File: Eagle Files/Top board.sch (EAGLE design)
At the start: 3 parts, among them J1 MINI-USB-5P-3400030P1, U1 CN3065-1320040P1

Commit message: Tweak board
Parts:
- removed J2: (no value), Connector:JST-2P-SMD'2.0'
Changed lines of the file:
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@@
 <setting verticaltext="up"/>
 </settings>
-<grid distance="0.1" unitdist="inch" unit="inch" style="lines" multiple="1" display="no" altdistance="0.01" altunitdist="inch" altunit="inch"/>
+<grid distance="5" unitdist="mil" unit="mil" style="lines" multiple="1" display="no" altdistance="1" altunitdist="mil" altunit="mil"/>
 <layers>
 <layer number="1" name="Top" color="4" fill="1" visible="no" active="no"/>
@@
 <part name="U1" library="IC" deviceset="CN3065" device="-1320040P1"/>
 <part name="J1" library="Connector" deviceset="MINI-USB-5P" device="-3400030P1"/>
-<part name="J2" library="Connector" deviceset="JST-2P-SMD" device="'2.0'"/>
 </parts>
 <sheets>
@@
 <instance part="U1" gate="U" x="73.66" y="58.42"/>
 <instance part="J1" gate="USB" x="40.64" y="40.64"/>
-<instance part="J2" gate="G$1" x="78.74" y="22.86"/>
 </instances>
 <busses>

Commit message: Tweaks
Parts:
- added RD2007: RD2007, radiationbean:RD2007
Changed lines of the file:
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@@
 <setting verticaltext="up"/>
 </settings>
-<grid distance="5" unitdist="mil" unit="mil" style="lines" multiple="1" display="no" altdistance="1" altunitdist="mil" altunit="mil"/>
+<grid distance="0.1" unitdist="inch" unit="inch" style="lines" multiple="1" display="no" altdistance="0.01" altunitdist="inch" altunit="inch"/>
 <layers>
 <layer number="1" name="Top" color="4" fill="1" visible="no" active="no"/>
@@
 <part name="U1" library="IC" deviceset="CN3065" device="-1320040P1"/>
 <part name="J1" library="Connector" deviceset="MINI-USB-5P" device="-3400030P1"/>
+<part name="RD2007" library="radiationbean" deviceset="RD2007" device=""/>
 </parts>
 <sheets>
@@
 <instance part="U1" gate="U" x="73.66" y="58.42"/>
 <instance part="J1" gate="USB" x="40.64" y="40.64"/>
+<instance part="RD2007" gate="G$1" x="35.56" y="60.96"/>
 </instances>
 <busses>
@@
 </schematic>
 </drawing>
+<compatibility>
+<note version="6.3" minversion="6.2.2" severity="warning">
+Since Version 6.2.2 text objects can contain more than one line,
+which will not be processed correctly with this version.
+</note>
+</compatibility>
 </eagle>

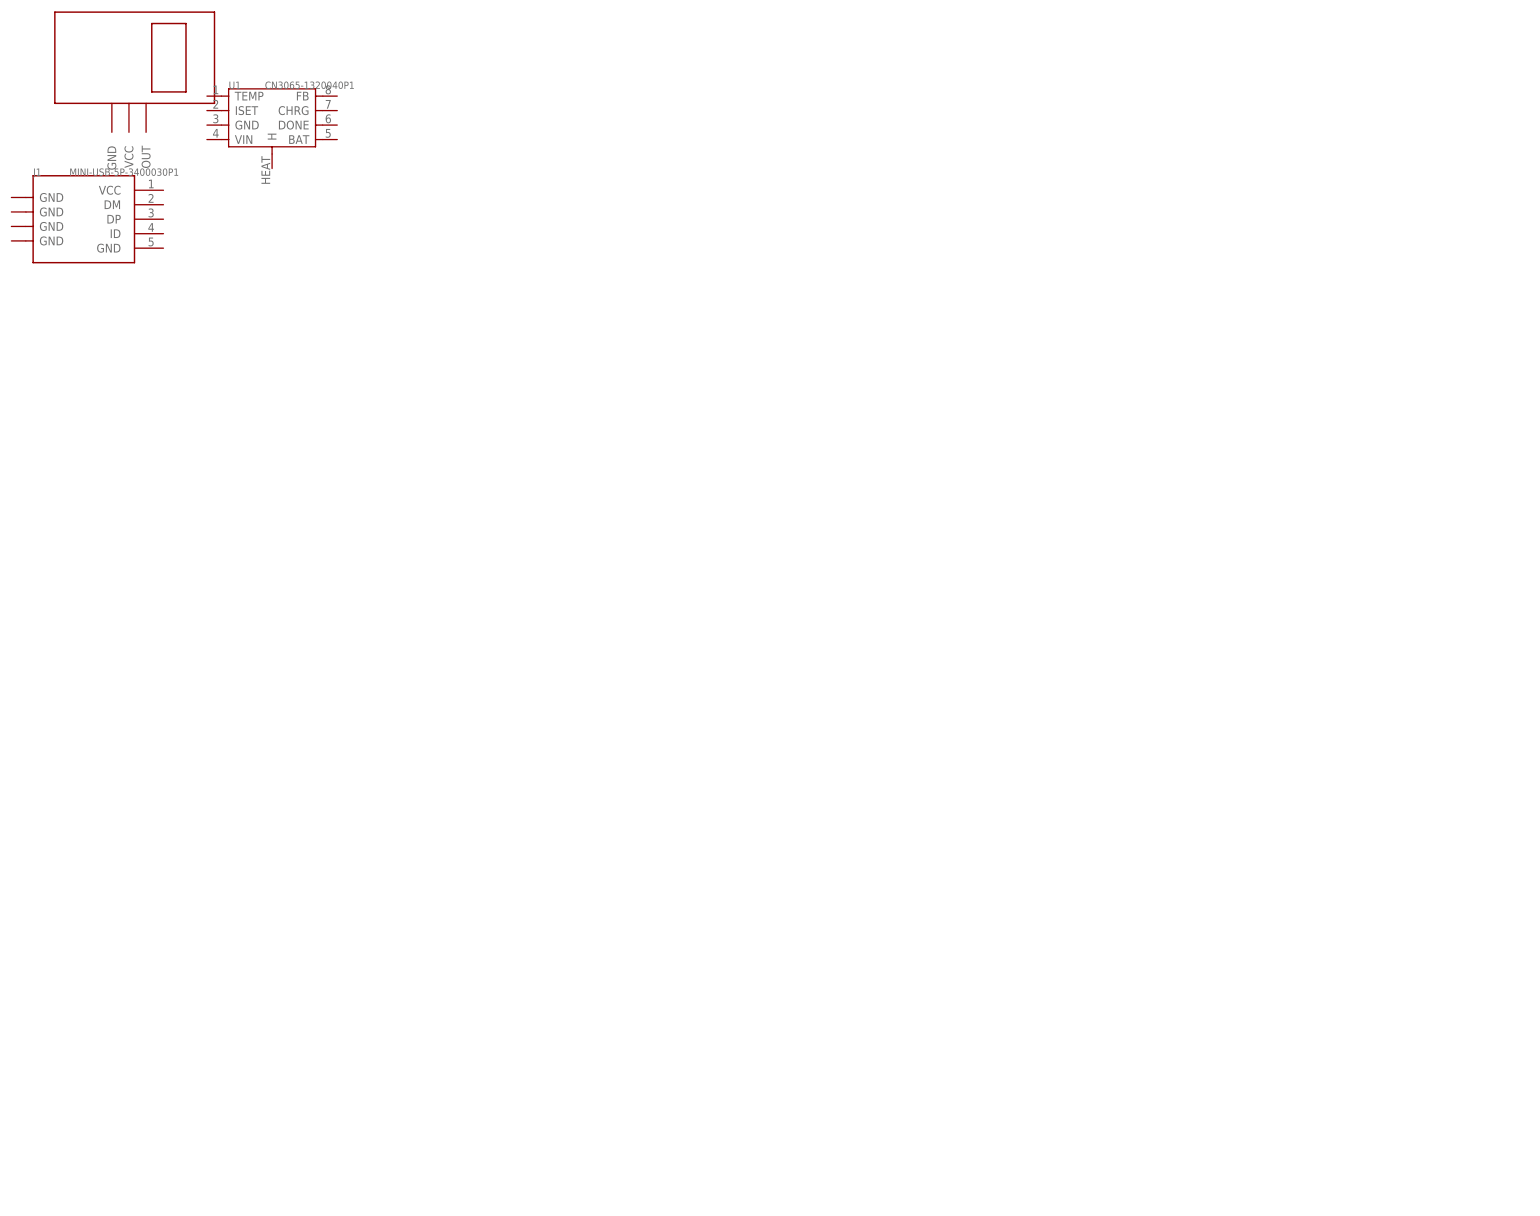
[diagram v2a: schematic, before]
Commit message: Renamed Eagle files.
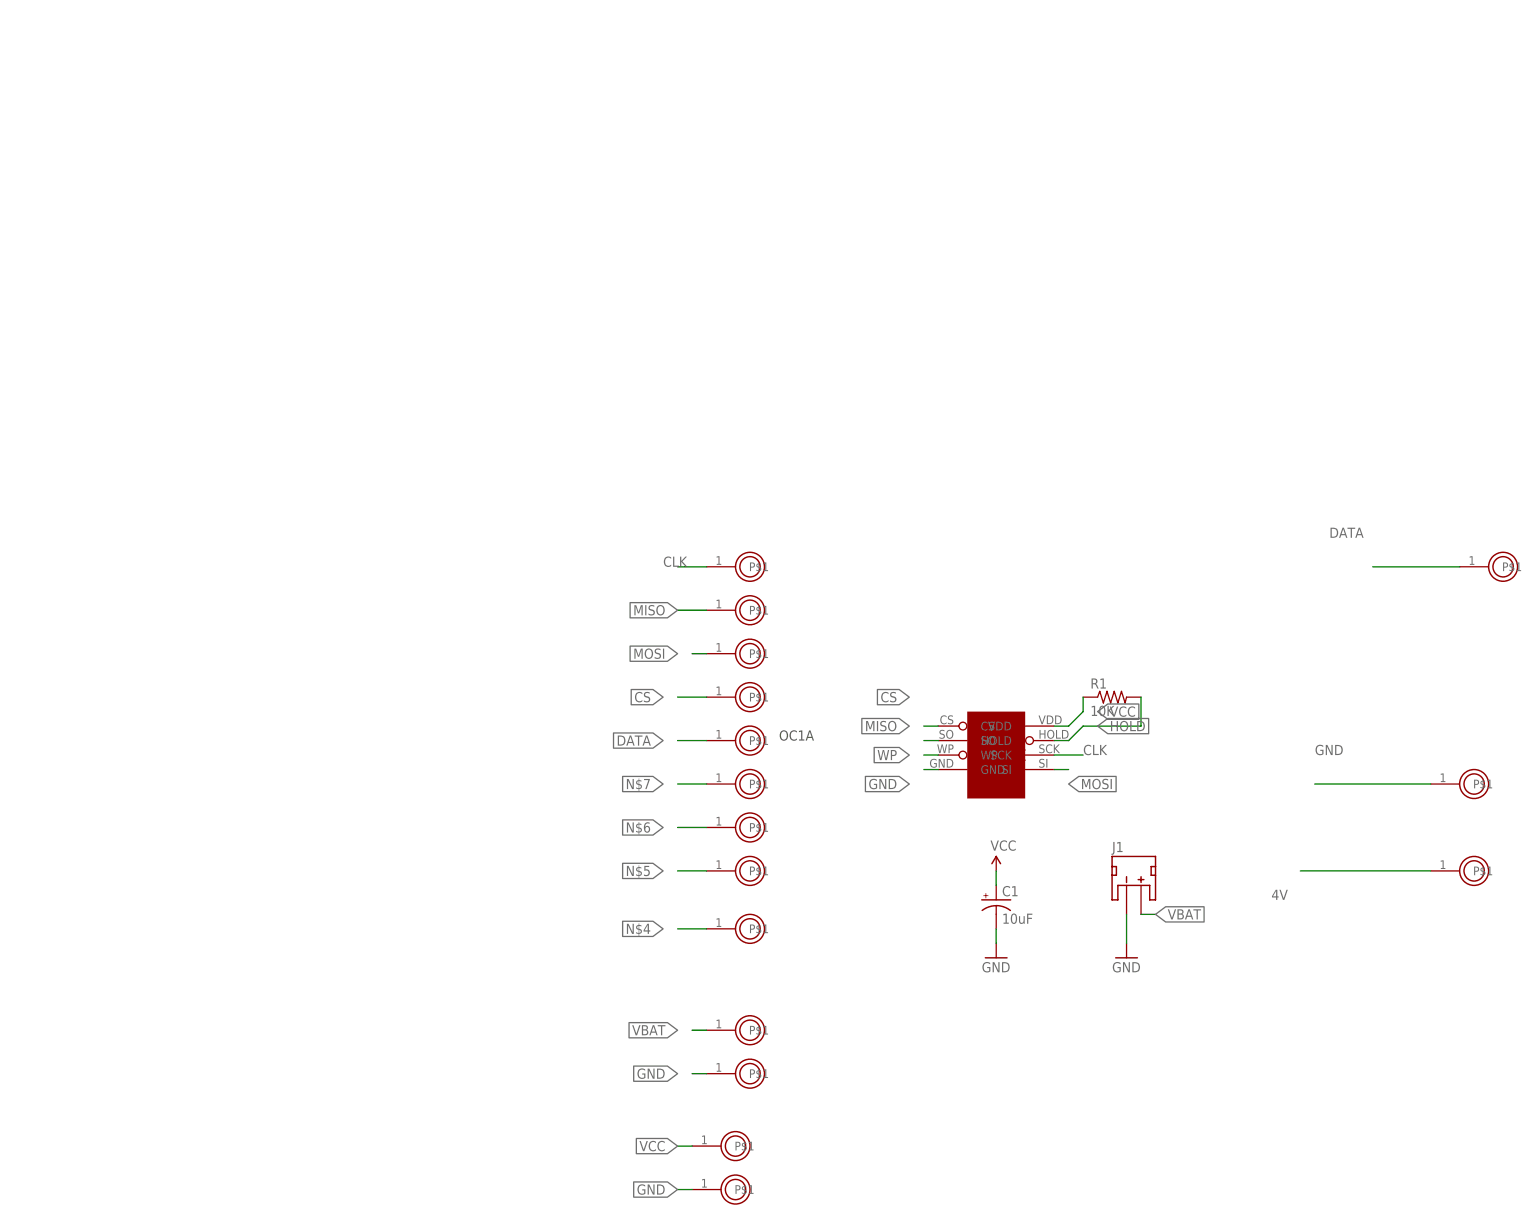
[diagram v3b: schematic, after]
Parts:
- removed RD2007: RD2007, radiationbean:RD2007
- removed U1: CN3065-1320040P1, IC:CN3065-1320040P1
- added 0, 1, 2, 3, 4, 4V, 5, A0, A1, BAT, DATA, GND@1, GND@2, GND@3, RESET, VCC: PROTO_POINT, BLEduino Bean:PROTO_POINT
- added C1: 10uF, SparkFun-Capacitors:10UF-16V-10%(TANT)
- added FRAM: MB85RS64V, radiationbean:MB85RS64V
- added R1: 10K, SparkFun-Resistors:10KOHM-1/10W-1%(0603)0603
- J1: value MINI-USB-5P-3400030P1 -> (none); device Connector:MINI-USB-5P-3400030P1 -> SparkFun-Connectors:JST_2MM_MALE
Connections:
- new net 4V: 4V.P$1
- new net CLK: 5.P$1, FRAM.SCK
- new net CS: 2.P$1, FRAM.CS
- new net DATA: 1.P$1, DATA.P$1
- new net GND: C1.-, FRAM.GND, GND@1.P$1, GND@2.P$1, GND@3.P$1, J1.-
- new net HOLD: FRAM.HOLD, R1.2
- new net MISO: 4.P$1, FRAM.SO
- new net MOSI: 3.P$1, FRAM.SI
- new net N$4: RESET.P$1
- new net N$5: A0.P$1
- new net N$6: A1.P$1
- new net N$7: 0.P$1
- new net VBAT: BAT.P$1, J1.+
- new net VCC: C1.+, FRAM.VDD, R1.1, VCC.P$1
- new net WP: FRAM.WP
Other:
- note added: "OC1A"

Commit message: v0.2
Switched to 32KB I2C Fram.
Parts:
- removed R1: 10K, SparkFun-Resistors:10KOHM-1/10W-1%(0603)0603
- FRAM: value MB85RS64V -> MB85RC256V; device radiationbean:MB85RS64V -> radiationbean:MB85RC256VMB85RC256V
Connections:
- removed net HOLD: FRAM.HOLD, R1.2
- removed net N$5: A0.P$1
- removed net N$6: A1.P$1
- new net A0: FRAM.V0
- new net A1: FRAM.A1
- new net A2: FRAM.A2
- new net SCL: A1.P$1, FRAM.SCL
- new net SDA: A0.P$1, FRAM.SDA
- net CLK: no longer FRAM.SCK
- net CS: no longer FRAM.CS
- net MISO: no longer FRAM.SO
- net MOSI: no longer FRAM.SI
- net VCC: no longer R1.1
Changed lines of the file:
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@@
 <part name="GND@3" library="BLEduino Bean" deviceset="PROTO_POINT" device=""/>
 <part name="RESET" library="BLEduino Bean" deviceset="PROTO_POINT" device=""/>
-<part name="FRAM" library="radiationbean" deviceset="MB85RS64V" device=""/>
-<part name="R1" library="SparkFun-Resistors" deviceset="10KOHM-1/10W-1%(0603)" device="0603" value="10K"/>
+<part name="FRAM" library="radiationbean" deviceset="MB85RC256V" device="MB85RC256V" value="MB85RC256V"/>
 <part name="C1" library="SparkFun-Capacitors" deviceset="10UF-16V-10%(TANT)" device="" value="10uF"/>
 <part name="GND1" library="SparkFun-Aesthetics" deviceset="GND" device=""/>
@@
 <instance part="GND@3" gate="G$1" x="149.86" y="-129.54"/>
 <instance part="RESET" gate="G$1" x="152.4" y="-83.82"/>
-<instance part="FRAM" gate="G$1" x="200.66" y="-53.34"/>
-<instance part="R1" gate="G$1" x="220.98" y="-43.18"/>
+<instance part="FRAM" gate="FRAM" x="200.66" y="-53.34"/>
 <instance part="C1" gate="G$1" x="200.66" y="-78.74"/>
 <instance part="GND1" gate="1" x="200.66" y="-88.9"/>
@@
 </segment>
 <segment>
-<pinref part="FRAM" gate="G$1" pin="GND"/>
+<pinref part="FRAM" gate="FRAM" pin="GND"/>
 <wire x1="190.5" y1="-55.88" x2="187.96" y2="-55.88" width="0.1524" layer="91"/>
 <label x="185.42" y="-58.42" size="1.778" layer="95" rot="R180" xref="yes"/>
@@
 <label x="142.24" y="-20.32" size="1.778" layer="95"/>
 </segment>
-<segment>
-<pinref part="FRAM" gate="G$1" pin="SCK"/>
-<wire x1="210.82" y1="-53.34" x2="215.9" y2="-53.34" width="0.1524" layer="91"/>
-<label x="215.9" y="-53.34" size="1.778" layer="95"/>
-</segment>
-</net>
-<net name="HOLD" class="0">
-<segment>
-<pinref part="FRAM" gate="G$1" pin="HOLD"/>
+</net>
+<net name="WP" class="0">
+<segment>
+<pinref part="FRAM" gate="FRAM" pin="WP"/>
 <wire x1="210.82" y1="-50.8" x2="213.36" y2="-50.8" width="0.1524" layer="91"/>
 <wire x1="213.36" y1="-50.8" x2="215.9" y2="-48.26" width="0.1524" layer="91"/>
 <label x="218.44" y="-48.26" size="1.778" layer="95" xref="yes"/>
-<pinref part="R1" gate="G$1" pin="2"/>
-<wire x1="215.9" y1="-48.26" x2="226.06" y2="-48.26" width="0.1524" layer="91"/>
-<wire x1="226.06" y1="-48.26" x2="226.06" y2="-43.18" width="0.1524" layer="91"/>
 </segment>
 </net>
@@
 </segment>
 <segment>
-<pinref part="FRAM" gate="G$1" pin="VDD"/>
+<pinref part="FRAM" gate="FRAM" pin="VDD"/>
 <wire x1="210.82" y1="-48.26" x2="213.36" y2="-48.26" width="0.1524" layer="91"/>
 <wire x1="213.36" y1="-48.26" x2="215.9" y2="-45.72" width="0.1524" layer="91"/>
 <label x="218.44" y="-45.72" size="1.778" layer="95" xref="yes"/>
-<pinref part="R1" gate="G$1" pin="1"/>
-<wire x1="215.9" y1="-45.72" x2="215.9" y2="-43.18" width="0.1524" layer="91"/>
 </segment>
 <segment>
@@
 </segment>
 </net>
-<net name="N$5" class="0">
+<net name="N$7" class="0">
+<segment>
+<wire x1="149.86" y1="-58.42" x2="144.78" y2="-58.42" width="0.1524" layer="91"/>
+<label x="142.24" y="-58.42" size="1.778" layer="95" rot="R180" xref="yes"/>
+<pinref part="0" gate="G$1" pin="P$1"/>
+</segment>
+</net>
+<net name="CS" class="0">
+<segment>
+<pinref part="2" gate="G$1" pin="P$1"/>
+<wire x1="149.86" y1="-43.18" x2="144.78" y2="-43.18" width="0.1524" layer="91"/>
+<label x="142.24" y="-43.18" size="1.778" layer="95" rot="R180" xref="yes"/>
+</segment>
+</net>
+<net name="MISO" class="0">
+<segment>
+<pinref part="4" gate="G$1" pin="P$1"/>
+<wire x1="149.86" y1="-27.94" x2="144.78" y2="-27.94" width="0.1524" layer="91"/>
+<label x="144.78" y="-27.94" size="1.778" layer="95" rot="R180" xref="yes"/>
+</segment>
+</net>
+<net name="A2" class="0">
+<segment>
+<pinref part="FRAM" gate="FRAM" pin="A2"/>
+<wire x1="190.5" y1="-53.34" x2="187.96" y2="-53.34" width="0.1524" layer="91"/>
+<label x="185.42" y="-53.34" size="1.778" layer="95" rot="R180" xref="yes"/>
+</segment>
+</net>
+<net name="MOSI" class="0">
+<segment>
+<pinref part="3" gate="G$1" pin="P$1"/>
+<wire x1="149.86" y1="-35.56" x2="147.32" y2="-35.56" width="0.1524" layer="91"/>
+<label x="144.78" y="-35.56" size="1.778" layer="95" rot="R180" xref="yes"/>
+</segment>
+</net>
+<net name="A0" class="0">
+<segment>
+<pinref part="FRAM" gate="FRAM" pin="V0"/>
+<wire x1="190.5" y1="-48.26" x2="187.96" y2="-48.26" width="0.1524" layer="91"/>
+<label x="185.42" y="-43.18" size="1.778" layer="95" rot="R180" xref="yes"/>
+</segment>
+</net>
+<net name="A1" class="0">
+<segment>
+<pinref part="FRAM" gate="FRAM" pin="A1"/>
+<wire x1="190.5" y1="-50.8" x2="187.96" y2="-50.8" width="0.1524" layer="91"/>
+<label x="185.42" y="-48.26" size="1.778" layer="95" rot="R180" xref="yes"/>
+</segment>
+</net>
+<net name="SCL" class="0">
+<segment>
+<pinref part="FRAM" gate="FRAM" pin="SCL"/>
+<wire x1="210.82" y1="-53.34" x2="215.9" y2="-53.34" width="0.1524" layer="91"/>
+<label x="215.9" y="-53.34" size="1.778" layer="95"/>
+</segment>
+<segment>
+<pinref part="A1" gate="G$1" pin="P$1"/>
+<wire x1="149.86" y1="-66.04" x2="144.78" y2="-66.04" width="0.1524" layer="91"/>
+<label x="142.24" y="-66.04" size="1.778" layer="95" rot="R180" xref="yes"/>
+</segment>
+</net>
+<net name="SDA" class="0">
+<segment>
+<pinref part="FRAM" gate="FRAM" pin="SDA"/>
+<wire x1="210.82" y1="-55.88" x2="213.36" y2="-55.88" width="0.1524" layer="91"/>
+<label x="213.36" y="-58.42" size="1.778" layer="95" xref="yes"/>
+</segment>
 <segment>
 <pinref part="A0" gate="G$1" pin="P$1"/>
@@
 </segment>
 </net>
-<net name="N$6" class="0">
-<segment>
-<pinref part="A1" gate="G$1" pin="P$1"/>
-<wire x1="149.86" y1="-66.04" x2="144.78" y2="-66.04" width="0.1524" layer="91"/>
-<label x="142.24" y="-66.04" size="1.778" layer="95" rot="R180" xref="yes"/>
-</segment>
-</net>
-<net name="N$7" class="0">
-<segment>
-<wire x1="149.86" y1="-58.42" x2="144.78" y2="-58.42" width="0.1524" layer="91"/>
-<label x="142.24" y="-58.42" size="1.778" layer="95" rot="R180" xref="yes"/>
-<pinref part="0" gate="G$1" pin="P$1"/>
-</segment>
-</net>
-<net name="CS" class="0">
-<segment>
-<pinref part="FRAM" gate="G$1" pin="CS"/>
-<wire x1="190.5" y1="-48.26" x2="187.96" y2="-48.26" width="0.1524" layer="91"/>
-<label x="185.42" y="-43.18" size="1.778" layer="95" rot="R180" xref="yes"/>
-</segment>
-<segment>
-<pinref part="2" gate="G$1" pin="P$1"/>
-<wire x1="149.86" y1="-43.18" x2="144.78" y2="-43.18" width="0.1524" layer="91"/>
-<label x="142.24" y="-43.18" size="1.778" layer="95" rot="R180" xref="yes"/>
-</segment>
-</net>
-<net name="MISO" class="0">
-<segment>
-<pinref part="FRAM" gate="G$1" pin="SO"/>
-<wire x1="190.5" y1="-50.8" x2="187.96" y2="-50.8" width="0.1524" layer="91"/>
-<label x="185.42" y="-48.26" size="1.778" layer="95" rot="R180" xref="yes"/>
-</segment>
-<segment>
-<pinref part="4" gate="G$1" pin="P$1"/>
-<wire x1="149.86" y1="-27.94" x2="144.78" y2="-27.94" width="0.1524" layer="91"/>
-<label x="144.78" y="-27.94" size="1.778" layer="95" rot="R180" xref="yes"/>
-</segment>
-</net>
-<net name="WP" class="0">
-<segment>
-<pinref part="FRAM" gate="G$1" pin="WP"/>
-<wire x1="190.5" y1="-53.34" x2="187.96" y2="-53.34" width="0.1524" layer="91"/>
-<label x="185.42" y="-53.34" size="1.778" layer="95" rot="R180" xref="yes"/>
-</segment>
-</net>
-<net name="MOSI" class="0">
-<segment>
-<pinref part="FRAM" gate="G$1" pin="SI"/>
-<wire x1="210.82" y1="-55.88" x2="213.36" y2="-55.88" width="0.1524" layer="91"/>
-<label x="213.36" y="-58.42" size="1.778" layer="95" xref="yes"/>
-</segment>
-<segment>
-<pinref part="3" gate="G$1" pin="P$1"/>
-<wire x1="149.86" y1="-35.56" x2="147.32" y2="-35.56" width="0.1524" layer="91"/>
-<label x="144.78" y="-35.56" size="1.778" layer="95" rot="R180" xref="yes"/>
-</segment>
-</net>
